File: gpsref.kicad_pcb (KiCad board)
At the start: 4 copper layers, 77.4 x 50 mm, 194 parts, among them J1 SMA, J11 Debug, J12 GPS_Snoop, J13 I2C_Snoop, J14 Boot, J2 SMA, J3 SMA, J4 SMA, J5 SMA, J6 USB_C_Receptacle_16P, Q1 AO3400A, Q2 AO3401A, SW1 Reset, T1 MABA-007159-000000, T2 MABA-007159-000000, U1 MAX-M10S, U11 74LVC1G125, U12 74LVC1G125, U13 TS5A23157DGS, U15 74LVC1G125, U2 TG5032CGN, U3 LMK05318BRGZR, U31 TMP117xxDRV, U4 STM32H503KBUx, U5 TPS82084SIL, U6 TPS82084SIL, U7 TPS7A8801RTJR, U9 TPS7A8801RTJR, Y1 32768Hz

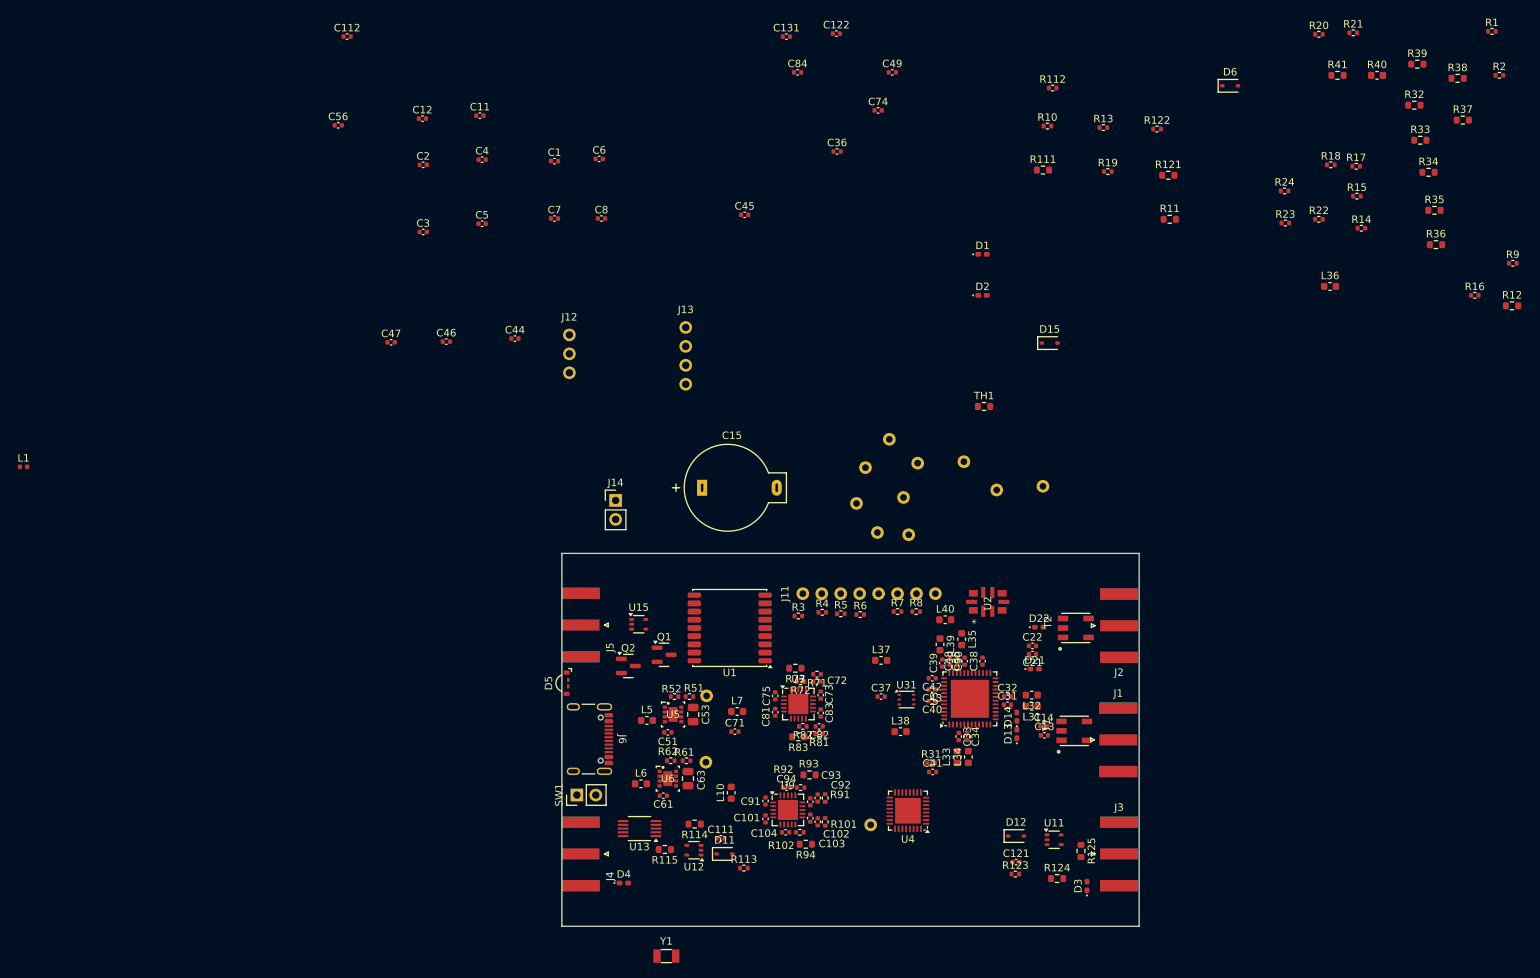
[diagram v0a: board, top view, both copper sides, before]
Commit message: First round of component distribution
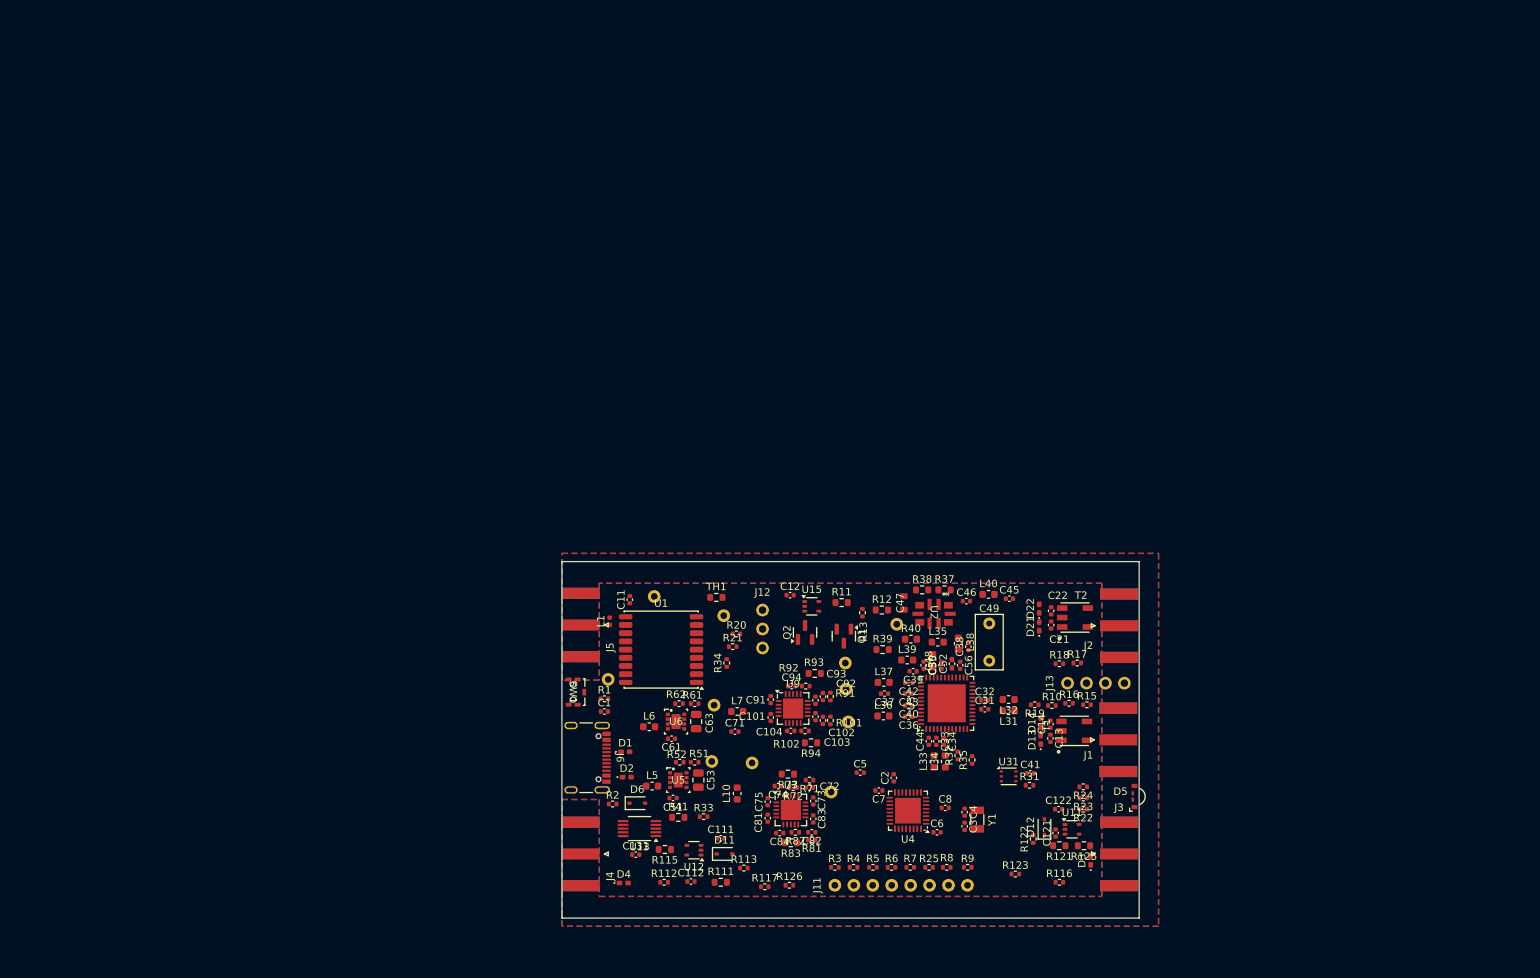
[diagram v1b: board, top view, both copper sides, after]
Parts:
- removed C15: 0F22, Capacitor_THT:DX_5R5HxxxxU_D11.5mm_P10.00mm
- removed D15: 1N4148WS, Diode_SMD:D_SOD-323
- removed J14: Boot, Connector_PinHeader_2.54mm:PinHeader_1x02_P2.54mm_Vertical
- removed R114, R124: 0, Resistor_SMD:R_0603_1608Metric
- removed R14: 1k, Resistor_SMD:R_0402_1005Metric
- removed R36: 1k, Resistor_SMD:R_0603_1608Metric
- removed TP31, TP32: TestPoint_Probe, Parts:TestPoint
- added C52: 10n, Capacitor_SMD:C_0402_1005Metric_Pad0.74x0.62mm_HandSolder, F.Cu at (152.3, 89.8)
- added R116: 100k, Resistor_SMD:R_0402_1005Metric, F.Cu at (166.7, 119.1)
- added R117: 100k, Resistor_SMD:R_0402_1005Metric, F.Cu at (127.2, 119.7)
- added R126: 100k, Resistor_SMD:R_0402_1005Metric, F.Cu at (130.5, 119.5)
- added R25: 10k, Resistor_SMD:R_0402_1005Metric, F.Cu at (149.2, 117.1)
- C47, C48: footprint Capacitor_SMD:C_0402_1005Metric -> Parts:C0704
- C49: footprint Capacitor_SMD:C_0402_1005Metric -> Capacitor_THT:C_Rect_L7.2mm_W3.5mm_P5.00mm_FKS2_FKP2_MKS2_MKP2
- R32, R33, R34, R35: footprint Resistor_SMD:R_0603_1608Metric -> Resistor_SMD:R_0402_1005Metric
- R9: value 10k -> 100
- SW1: footprint Connector_PinHeader_2.54mm:PinHeader_1x02_P2.54mm_Vertical -> Parts:SOU-242HNT_MIT
- moved R2 153.9 mm to (106.8, 108.6)
- moved R1 148.9 mm to (105.7, 94.5)
- moved R41 133.1 mm to (115.6, 110.4)
- moved R33 132.1 mm to (119.0, 110.3)
- moved D6 124.8 mm to (110.1, 108.5)
- moved C112 122.3 mm to (117.3, 119.0)
- moved R112 118.6 mm to (113.7, 119.1)
- moved R21 117.0 mm to (122.9, 87.5)
- moved R34 114.8 mm to (122.1, 89.7), turned to 90 degrees
- moved R20 112.1 mm to (123.4, 85.8)
- moved C131 111.5 mm to (109.9, 115.4)
- moved C56 110.4 mm to (153.4, 90.0), turned to -90 degrees
- moved R9 109.1 mm to (154.4, 117.1)
- moved C4 108.8 mm to (154.0, 109.7), turned to -90 degrees
- moved C122 108.2 mm to (166.6, 109.3)
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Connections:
- net Net-(C11-Pad1) renamed /GPS/VrfSW
- net Net-(J12-Pin_1) renamed /CPU/SCG
- net Net-(J12-Pin_2) renamed /CPU/SGC
- net Net-(J13-Pin_1) renamed /CPU/sSCL
- net Net-(J13-Pin_2) renamed /CPU/sSDA
- net Net-(J13-Pin_3) renamed /CPU/sPDN
- net Net-(J6-CC1) renamed /CPU/CC1
- net Net-(J6-CC2) renamed /CPU/CC2
- net Net-(Q1-G) renamed /GPS/LNA_EN
- net Net-(Q2-S) renamed /GPS/Vrf
- net Net-(U1-VCC_RF) renamed /GPS/VCC_RF
- net Net-(U2A-Filter) renamed /Clocking/XO_Filter
- net Net-(U2A-VCC) renamed /Clocking/VCC_XO
- net Net-(U3-CAP_PLL1) renamed /Clocking/CAP_PLL1
- net Net-(U3-CAP_PLL2) renamed /Clocking/CAP_PLL2
- net Net-(U3-LF1) renamed /Clocking/LF1
- net Net-(U3-LF2) renamed /Clocking/LF2
- net Net-(U3-PRIREF_P) renamed /Clocking/GPSCLKLO
- net Net-(U3-SECREF_P) renamed /Clocking/SecRefLo
- net Net-(U4-PC14) renamed /CPU/X32In
- net Net-(U4-PC15) renamed /CPU/X32Out
- J11 pad 5: unconnected-(J11-Pin_5-Pad5) -> /CPU/dBOOT
- R7 pad 1: /CPU/dSWC -> /CPU/dBOOT
- R7 pad 2: /CPU/SWCLK -> /CPU/BOOT0
- R8 pad 1: /CPU/dSWD -> /CPU/dSWC
- R8 pad 2: /CPU/SWDIO -> /CPU/SWCLK
- R9 pad 1: /CPU/BOOT0 -> /CPU/dSWD
- R9 pad 2: GND -> /CPU/SWDIO
- U1 pad 6: /GPS/V_BCKP -> +3V3
- U11 pad 1: EN_OUT3 -> EN_OUT4
- U11 pad 2: Net-(D12-A) -> Net-(D11-A)
- U11 pad 4: Net-(R125-Pad1) -> Net-(R115-Pad1)
- U12 pad 1: EN_OUT4 -> EN_OUT3
- U12 pad 2: Net-(D11-A) -> Net-(D12-A)
- U12 pad 4: Net-(R115-Pad1) -> Net-(R125-Pad1)
- U13 pad 4: /Outputs/Conn4 -> SecRef
- U13 pad 6: SecRef -> /Outputs/Conn4
- U3 pad 12: Net-(U3-GPIO0) -> /Clocking/VDD_DIG
- U3 pad 13: ~{PD} -> PDN
- U3 pad 30: GPIO2 -> GND
- U4 pad 18: ~{PD} -> PDN
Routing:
- added copper zone on B.Cu, net GND
- added copper zone on F.Cu, net GND
- added copper zone on In1.Cu, net GND
- added copper zone on In2.Cu, net GND
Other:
- board size 77.4 x 50 mm -> 77.4 x 47.8 mm

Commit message: Placement looks sane.
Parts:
- D5: value LED_BGKR -> LED_GBAR; footprint LED_SMD:LED_RGB_Everlight_EASV3015RGBA0_Horizontal -> Parts:LED-QPLB615-RGB
- U11, U12: footprint Package_TO_SOT_SMD:SOT-353_SC-70-5 -> Package_TO_SOT_SMD:SOT-23-5
- U13: value TS5A23157DGS -> TS5A63157DBV; footprint Package_SO:VSSOP-10_3x3mm_P0.5mm -> Package_TO_SOT_SMD:SOT-23-6
- U15: value 74LVC1G125 -> 74LVC1G07; footprint Package_TO_SOT_SMD:SOT-353_SC-70-5 -> Package_TO_SOT_SMD:SOT-23-5
- moved U11 54.1 mm to (114.4, 116.0), turned to 180 degrees
- moved U12 51.2 mm to (168.8, 111.6), turned to 0 degrees
- moved R12 33.4 mm to (111.9, 95.1), turned to 180 degrees
- moved R11 31.7 mm to (108.8, 95.1)
- moved U15 22.4 mm to (111.1, 80.8)
- moved C84 19.3 mm to (126.1, 93.4)
- moved R13 19.3 mm to (121.1, 80.5), turned to -90 degrees
- moved R82 19.3 mm to (128.1, 93.4)
- moved R81 18.5 mm to (132.2, 94.9), turned to 90 degrees
- moved C82 17.7 mm to (131.2, 94.9), turned to 90 degrees
- moved TP13 16.8 mm to (121.2, 89.2), turned to 90 degrees
- moved C12 16.5 mm to (114.1, 80.3), turned to -90 degrees
- moved C83 15.6 mm to (130.2, 95.4), turned to 90 degrees
- moved C81 15.5 mm to (124.0, 95.4), turned to 90 degrees
- moved J12 15.3 mm to (138.5, 92.5)
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- renumbered J2 to J1, J1 to J2
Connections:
- C104 pad 1: Net-(U9B-NR_SS2) -> Net-(U7A-NR_SS1)
- C74 pad 1: Net-(U7A-NR_SS1) -> Net-(U7B-NR_SS2)
- C84 pad 1: Net-(U7B-NR_SS2) -> Net-(U9A-NR_SS1)
- C94 pad 1: Net-(U9A-NR_SS1) -> Net-(U9B-NR_SS2)
- D5 pad 1: Net-(D5-BA) -> Net-(D5-GK)
- D5 pad 2: Net-(D5-GA) -> Net-(D5-BK)
- D5 pad 3: GND -> +3V3
- R22 pad 1: Net-(D5-BA) -> Net-(D5-BK)
- R22 pad 2: /CPU/Red -> /CPU/Blue
- R23 pad 1: Net-(D5-GA) -> Net-(D5-GK)
- R24 pad 2: /CPU/Blue -> /CPU/Red
- U1 pad 16: I2C_SDA -> I2C_SCL
- U1 pad 17: I2C_SCL -> I2C_SDA
- U13 pad 1: EN_OUT4 -> SecRef
- U13 pad 2: unconnected-(U13-Pad2) -> GND
- U13 pad 3: GND -> /Outputs/Ext4
- U13 pad 4: SecRef -> /Outputs/Conn4
- U13 pad 5: EN_REF2 -> +3V3
- U13 pad 6: /Outputs/Conn4 -> EN_REF2
- U15 pad 1: GND -> unconnected-(U15-NC-Pad1)
- U4 pad 10: /CPU/DBG_TX -> STATUS1
- U4 pad 11: EN_OUT3 -> /CPU/DBG_TX
- U4 pad 12: Alert -> STATUS0
- U4 pad 13: unconnected-(U4-PA7-Pad13) -> PDN
- U4 pad 14: /CPU/Red -> CPU2GPS
- U4 pad 15: GPS_nRST -> GPS2CPU
- U4 pad 18: PDN -> GPIO2
- U4 pad 19: /CPU/Blue -> GPS_nRST
- U4 pad 25: /CPU/Green -> /CPU/DBG_RX
- U4 pad 26: I2C_SCL -> EN_OUT4
- U4 pad 27: I2C_SDA -> EN_REF2
- U4 pad 28: EN_OUT4 -> unconnected-(U4-PB5-Pad28)
- U4 pad 29: CPU2GPS -> I2C_SCL
- U4 pad 30: GPS2CPU -> I2C_SDA
- U4 pad 32: EN_REF2 -> EN_OUT3
- U4 pad 6: STATUS0 -> /CPU/Green
- U4 pad 7: STATUS1 -> /CPU/Red
- U4 pad 8: GPIO2 -> /CPU/Blue
- U4 pad 9: /CPU/DBG_RX -> Alert
- U7 pad 1: /Power/In3V3 -> /Power/In1V8
- U7 pad 10: /Power/FbTC3 -> /Power/Fb3V3
- U7 pad 11: TCXO_3V3 -> +3V3
- U7 pad 12: TCXO_3V3 -> +3V3
- U7 pad 14: +3V3 -> CGEN_1V8
- U7 pad 15: +3V3 -> CGEN_1V8
- U7 pad 16: /Power/Fb3V3 -> /Power/FbCG18
- U7 pad 2: /Power/In3V3 -> /Power/In1V8
- U7 pad 20: /Power/In3V3 -> /Power/In1V8
- U9 pad 10: /Power/FbCG18 -> /Power/FbCG3
- U9 pad 11: CGEN_1V8 -> CGEN_3V3
- U9 pad 12: CGEN_1V8 -> CGEN_3V3
- U9 pad 14: CGEN_3V3 -> TCXO_3V3
- U9 pad 15: CGEN_3V3 -> TCXO_3V3
- U9 pad 16: /Power/FbCG3 -> /Power/FbTC3
- U9 pad 4: /Power/In1V8 -> /Power/In3V3
- U9 pad 5: /Power/In1V8 -> /Power/In3V3
- U9 pad 6: /Power/In1V8 -> /Power/In3V3
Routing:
- net /CPU/USB_D-: track 0.00 -> 44.6 mm
- net /CPU/USB_D+: track 0.00 -> 44.5 mm

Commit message: Routing well underway
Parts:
- removed R10, R15, R16: 100, Resistor_SMD:R_0402_1005Metric
- removed R19: 100k, Resistor_SMD:R_0402_1005Metric
- removed SW1: Reset, Parts:SOU-242HNT_MIT
- removed TP11: TestPoint_Probe, Parts:TestPoint
- added R118: 0, Resistor_SMD:R_0603_1608Metric, F.Cu at (107.4, 115.2)
- D1, D13, D14, D2, D21, D22, D3: footprint Diode_SMD:D_0402_1005Metric_Pad0.77x0.64mm_HandSolder -> Parts:HHS_0402
- D4: value D_TVS -> BAS40-04; footprint Diode_SMD:D_0402_1005Metric_Pad0.77x0.64mm_HandSolder -> Package_TO_SOT_SMD:SOT-23
- L1: footprint Inductor_SMD:L_0402_1005Metric -> Parts:HHS_0402
- R37, R38, R39: footprint Resistor_SMD:R_0603_1608Metric -> Resistor_SMD:R_0402_1005Metric
- R40: footprint Inductor_SMD:L_0603_1608Metric -> Resistor_SMD:R_0402_1005Metric
- U11: value 74LVC1G125 -> 74LVC1G240
- U31: footprint Parts:WSON-6-1EP_2x2mm_P0.65mm_NoEP -> Package_SON:WSON-6-1EP_2x2mm_P0.65mm_EP1x1.6mm
- moved R116 43.3 mm to (123.5, 119.8)
- moved R126 18.8 mm to (148.7, 114.8), turned to -90 degrees
- moved L40 17.9 mm to (139.3, 79.8)
- moved R9 17.8 mm to (136.6, 117.1), turned to 180 degrees
- moved J11 17.8 mm to (154.4, 119.5), turned to -90 degrees
- moved R3 17.8 mm to (154.4, 117.1), turned to 180 degrees
- moved R17 14.6 mm to (162.9, 102.9)
- moved J13 13.9 mm to (162.4, 105.2)
- moved R18 13.2 mm to (164.8, 102.9), turned to 180 degrees
- moved R4 12.7 mm to (151.8, 117.1), turned to 180 degrees
- moved R8 12.5 mm to (139.1, 117.1), turned to 180 degrees
- moved R123 11.2 mm to (166.2, 108.2)
- moved C46 10.5 mm to (143.7, 81.1), turned to 90 degrees
- moved C1 10.0 mm to (108.2, 105.9)
- moved TP8 8.97 mm to (136.8, 88.5)
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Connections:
- D1 pad 1: GND -> /CPU/USB_D+
- D1 pad 2: /CPU/USB_D+ -> GND
- D13 pad 1: GND -> OUT0_P
- D13 pad 2: OUT0_P -> GND
- D2 pad 1: GND -> /CPU/USB_D-
- D2 pad 2: /CPU/USB_D- -> GND
- D21 pad 1: GND -> OUT2_P
- D21 pad 2: OUT2_P -> GND
- D3 pad 1: GND -> /Outputs/Ext3
- D3 pad 2: /Outputs/Ext3 -> GND
- D4 pad 2: /Outputs/Conn4 -> +3V3
- J13 pad 1: /CPU/sSCL -> I2C_SDA
- J13 pad 2: /CPU/sSDA -> I2C_SCL
- J13 pad 3: /CPU/sPDN -> PDN
- R17 pad 1: I2C_SCL -> I2C_SDA
- R18 pad 1: I2C_SDA -> I2C_SCL
- TP13 pad 1: GPSCLK -> /Clocking/GPSCLKLO
- U1 pad 16: I2C_SCL -> unconnected-(U1-SDA-Pad16)
- U1 pad 17: I2C_SDA -> unconnected-(U1-SCL-Pad17)
- U1 pad 18: Net-(U1-~{SAFEBOOT}) -> unconnected-(U1-~{SAFEBOOT}-Pad18)
- U1 pad 6: +3V3 -> unconnected-(U1-V_BCKP-Pad6)
- U13 pad 4: /Outputs/Conn4 -> Net-(D4-Pad3)
- U4 pad 10: STATUS1 -> PDN
- U4 pad 12: STATUS0 -> STATUS1
- U4 pad 13: PDN -> unconnected-(U4-PA7-Pad13)
- U4 pad 14: CPU2GPS -> STATUS0
- U4 pad 15: GPS2CPU -> GPS_nRST
- U4 pad 18: GPIO2 -> GPS2CPU
- U4 pad 19: GPS_nRST -> CPU2GPS
- U4 pad 6: /CPU/Green -> /CPU/Blue
- U4 pad 7: /CPU/Red -> /CPU/Green
- U4 pad 8: /CPU/Blue -> /CPU/Red
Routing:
- net +3V3: track 0.00 -> 197.0 mm, vias 0 -> 10
- net CGEN_3V3: track 0.00 -> 94.5 mm, vias 0 -> 10
- net CGEN_1V8: track 0.00 -> 58.4 mm, vias 0 -> 4
- net I2C_SCL: track 0.00 -> 54.5 mm, vias 0 -> 4
- net GND: track 0.00 -> 52.3 mm, vias 0 -> 59
- net PDN: track 0.00 -> 49.9 mm, vias 0 -> 2
- net I2C_SDA: track 0.00 -> 48.7 mm, vias 0 -> 5
- net OUT7_N: track 0.00 -> 42.8 mm, vias 0 -> 2
- net GPS_nRST: track 0.00 -> 42.5 mm, vias 0 -> 2
- net /Clocking/GPSCLKLO: track 0.00 -> 39.7 mm, vias 0 -> 2
- net CPU2GPS: track 0.00 -> 39.4 mm, vias 0 -> 2
- net GPS2CPU: track 0.00 -> 36.9 mm
- net OUT7_P: track 0.00 -> 35.8 mm, vias 0 -> 2
- net /CPU/Blue: track 0.00 -> 31.1 mm
- net EN_REF2: track 0.00 -> 31.0 mm, vias 0 -> 2
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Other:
- outline, holes or cut-outs redrawn
